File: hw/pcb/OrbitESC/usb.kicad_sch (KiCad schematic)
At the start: 5 parts, among them J1 USB_C_Receptacle_USB2.0

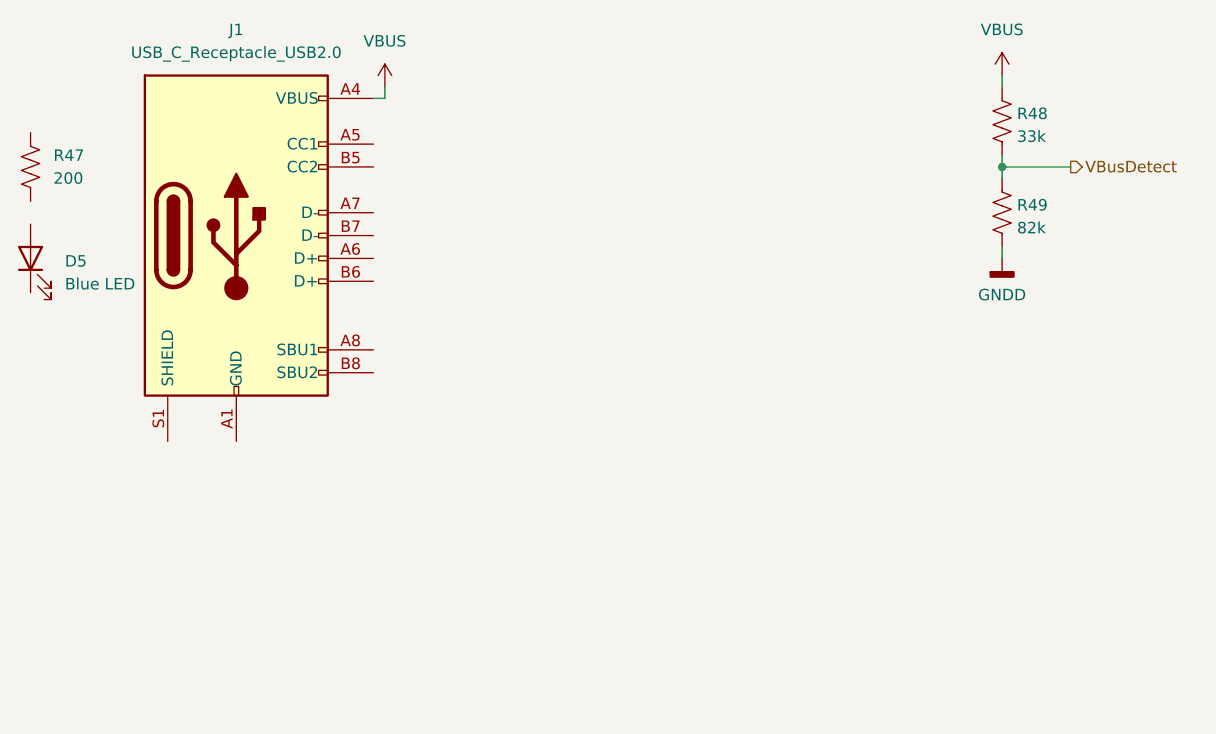
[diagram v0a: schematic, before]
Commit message: Connect USB to MCU
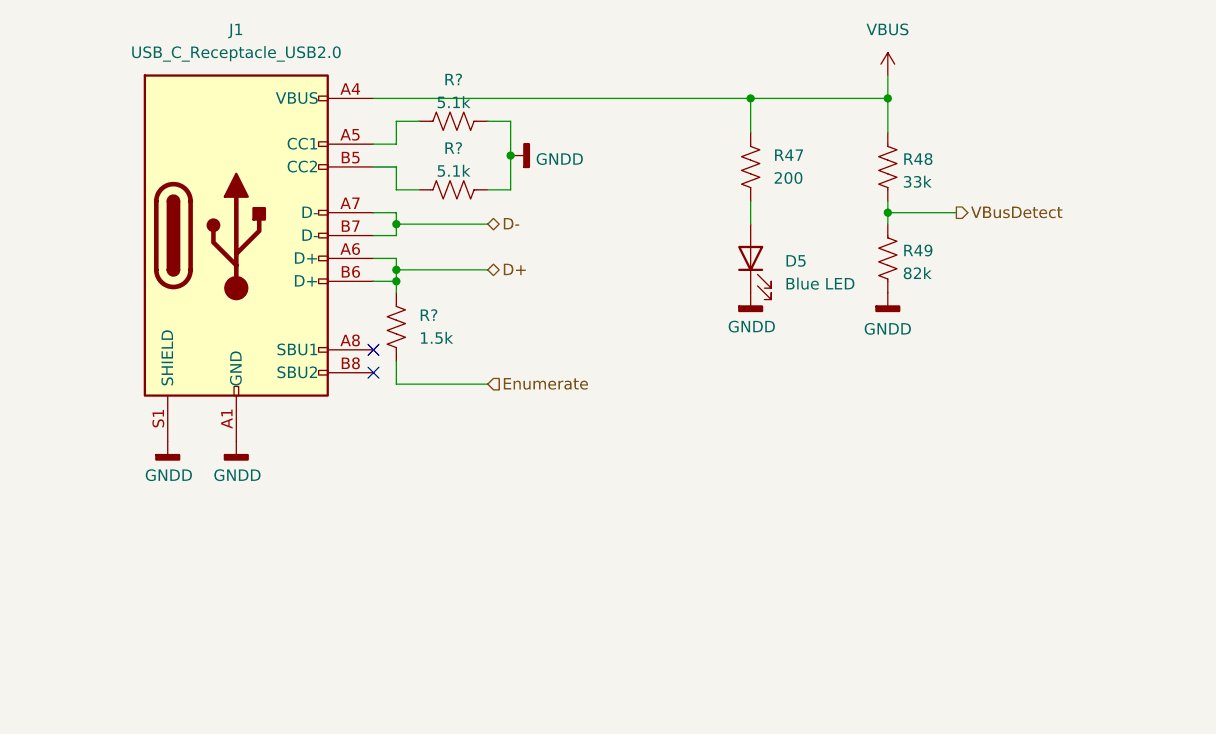
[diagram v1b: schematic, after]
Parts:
- added R? (x2): 5.1k, Resistor_SMD:R_0402_1005Metric, symbol Device:R_US
- added R?: 1.5k, Resistor_SMD:R_0402_1005Metric, symbol Device:R_US
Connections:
- net GNDD: now also D5.1 (K), J1.A1 (GND), J1.A12 (GND), J1.B1 (GND), J1.B12 (GND), J1.S1 (SHIELD), R?.2, R?.2
- net VBUS: now also R47.1
- net at R47.2: now also D5.2 (A)
- net at J1.A5 (CC1): now also R?.1
- net D+: now reaches J1.A6 (D+)
- net D+: now also J1.B6 (D+), R?.1
- net D-: now reaches J1.A7 (D-)
- net D-: now also J1.B7 (D-)
- net at J1.B5 (CC2): now also R?.1
- new net Enumerate: R?.2
- no-connect marks 0 -> 2
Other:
- moved on the sheet: D5, R47, R48, R49

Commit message: Fill out majority of schematic
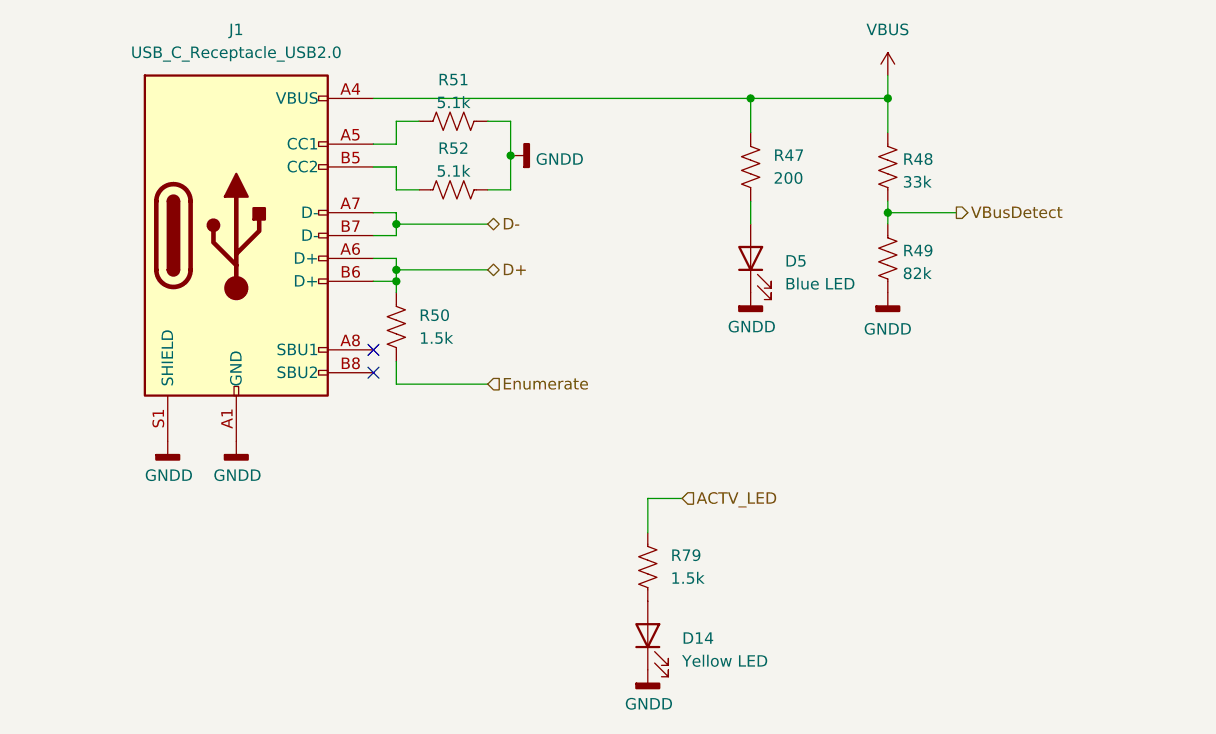
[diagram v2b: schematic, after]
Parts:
- added D14: Yellow LED, Diode_SMD:D_0603_1608Metric, symbol Device:LED
- added R79: 1.5k, Resistor_SMD:R_0402_1005Metric, symbol Device:R_US
- gave numbers to parts that had none: 3
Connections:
- net GNDD: now also D14.1 (K)
- new net: D14.2 (A), R79.2
- new net ACTV_LED: R79.1
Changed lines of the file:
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@@
+    (stroke (width 0) (type default) (color 0 0 0 0))
+  )
+  (wire (pts (xy 119.38 99.06) (xy 123.19 99.06))
     (stroke (width 0) (type default) (color 0 0 0 0))
   )
@@
     (stroke (width 0) (type default) (color 0 0 0 0))
   )
+  (wire (pts (xy 119.38 99.06) (xy 119.38 102.87))
+    (stroke (width 0) (type default) (color 0 0 0 0))
+  )
   (hierarchical_label "D-" (shape bidirectional) (at 101.6 68.58 0)
     (effects (font (size 1.27 1.27)) (justify left))
@@
     (effects (font (size 1.27 1.27)) (justify left))
   )
+  (hierarchical_label "ACTV_LED" (shape input) (at 123.19 99.06 0)
+    (effects (font (size 1.27 1.27)) (justify left))
+  )
   (hierarchical_label "D+" (shape bidirectional) (at 101.6 73.66 0)
     (effects (font (size 1.27 1.27)) (justify left))
@@
   (symbol (lib_id "Device:R_US") (at 97.79 64.77 90) (unit 1)
     (in_bom yes) (on_board yes) (fields_autoplaced)
-    (property "Reference" "R?" (id 0) (at 97.79 60.1812 90))
+    (property "Reference" "R52" (id 0) (at 97.79 60.1812 90))
     (property "Value" "5.1k" (id 1) (at 97.79 62.7181 90))
     (property "Footprint" "Resistor_SMD:R_0402_1005Metric" (id 2) (at 98.044 63.754 90)
@@
   (symbol (lib_id "Device:R_US") (at 97.79 57.15 90) (unit 1)
     (in_bom yes) (on_board yes) (fields_autoplaced)
-    (property "Reference" "R?" (id 0) (at 97.79 52.5612 90))
+    (property "Reference" "R51" (id 0) (at 97.79 52.5612 90))
     (property "Value" "5.1k" (id 1) (at 97.79 55.0981 90))
     (property "Footprint" "Resistor_SMD:R_0402_1005Metric" (id 2) (at 98.044 56.134 90)
@@
     (pin "2")
   )
+  (symbol (lib_id "power:GNDD") (at 119.38 118.11 0) (unit 1)
+    (in_bom yes) (on_board yes)
+    (property "Reference" "#PWR0128" (id 0) (at 119.38 124.46 0)
+      (effects (font (size 1.27 1.27)) hide)
+    )
+    (property "Value" "GNDD" (id 1) (at 116.84 121.92 0)
+      (effects (font (size 1.27 1.27)) (justify left))
+    )
+    (property "Footprint" "" (id 2) (at 119.38 118.11 0)
+      (effects (font (size 1.27 1.27)) hide)
+    )
+    (property "Datasheet" "" (id 3) (at 119.38 118.11 0)
+      (effects (font (size 1.27 1.27)) hide)
+    )
+    (pin "1")
+  )
   (symbol (lib_id "power:GNDD") (at 66.04 92.71 0) (unit 1)
     (in_bom yes) (on_board yes)
-    (property "Reference" "#PWR?" (id 0) (at 66.04 99.06 0)
+    (property "Reference" "#PWR040" (id 0) (at 66.04 99.06 0)
       (effects (font (size 1.27 1.27)) hide)
     )
@@
   (symbol (lib_id "Device:R_US") (at 91.44 80.01 0) (unit 1)
     (in_bom yes) (on_board yes) (fields_autoplaced)
-    (property "Reference" "R?" (id 0) (at 93.98 78.7399 0)
+    (property "Reference" "R50" (id 0) (at 93.98 78.7399 0)
       (effects (font (size 1.27 1.27)) (justify left))
     )
@@
   (symbol (lib_id "power:GNDD") (at 73.66 92.71 0) (unit 1)
     (in_bom yes) (on_board yes)
-    (property "Reference" "#PWR?" (id 0) (at 73.66 99.06 0)
+    (property "Reference" "#PWR044" (id 0) (at 73.66 99.06 0)
       (effects (font (size 1.27 1.27)) hide)
     )
@@
     (pin "1")
   )
+  (symbol (lib_id "Device:R_US") (at 119.38 106.68 0) (unit 1)
+    (in_bom yes) (on_board yes) (fields_autoplaced)
+    (property "Reference" "R79" (id 0) (at 121.92 105.4099 0)
+      (effects (font (size 1.27 1.27)) (justify left))
+    )
+    (property "Value" "1.5k" (id 1) (at 121.92 107.9499 0)
+      (effects (font (size 1.27 1.27)) (justify left))
+    )
+    (property "Footprint" "Resistor_SMD:R_0402_1005Metric" (id 2) (at 120.396 106.934 90)
+      (effects (font (size 1.27 1.27)) hide)
+    )
+    (property "Datasheet" "~" (id 3) (at 119.38 106.68 0)
+      (effects (font (size 1.27 1.27)) hide)
+    )
+    (property "JLCPCB" "C25867" (id 4) (at 119.38 106.68 0)
+      (effects (font (size 1.27 1.27)) hide)
+    )
+    (pin "1")
+    (pin "2")
+  )
   (symbol (lib_id "Device:LED") (at 130.81 72.39 90) (unit 1)
     (in_bom yes) (on_board yes) (fields_autoplaced)
@@
   (symbol (lib_id "power:GNDD") (at 130.81 76.2 0) (unit 1)
     (in_bom yes) (on_board yes)
-    (property "Reference" "#PWR?" (id 0) (at 130.81 82.55 0)
+    (property "Reference" "#PWR046" (id 0) (at 130.81 82.55 0)
       (effects (font (size 1.27 1.27)) hide)
     )
@@
   (symbol (lib_id "power:GNDD") (at 104.14 60.96 90) (unit 1)
     (in_bom yes) (on_board yes) (fields_autoplaced)
-    (property "Reference" "#PWR?" (id 0) (at 110.49 60.96 0)
+    (property "Reference" "#PWR045" (id 0) (at 110.49 60.96 0)
       (effects (font (size 1.27 1.27)) hide)
     )
@@
     (pin "1")
   )
+  (symbol (lib_id "Device:LED") (at 119.38 114.3 90) (unit 1)
+    (in_bom yes) (on_board yes) (fields_autoplaced)
+    (property "Reference" "D14" (id 0) (at 123.19 114.6174 90)
+      (effects (font (size 1.27 1.27)) (justify right))
+    )
+    (property "Value" "Yellow LED" (id 1) (at 123.19 117.1574 90)
+      (effects (font (size 1.27 1.27)) (justify right))
+    )
+    (property "Footprint" "Diode_SMD:D_0603_1608Metric" (id 2) (at 119.38 114.3 0)
+      (effects (font (size 1.27 1.27)) hide)
+    )
+    (property "Datasheet" "~" (id 3) (at 119.38 114.3 0)
+      (effects (font (size 1.27 1.27)) hide)
+    )
+    (property "JLCPCB" "C72038" (id 4) (at 119.38 114.3 90)
+      (effects (font (size 1.27 1.27)) hide)
+    )
+    (pin "1")
+    (pin "2")
+  )
   (symbol (lib_id "Device:R_US") (at 146.05 62.23 0) (unit 1)

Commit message: Schematic checklist runthrough
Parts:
- R48: footprint (none) -> Resistor_SMD:R_0402_1005Metric; JLCPCB (none) -> C25779
- R49: footprint (none) -> Resistor_SMD:R_0603_1608Metric; JLCPCB (none) -> C23254
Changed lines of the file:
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@@
       (effects (font (size 1.27 1.27)) (justify left))
     )
-    (property "Footprint" "" (id 2) (at 147.066 72.644 90)
+    (property "Footprint" "Resistor_SMD:R_0603_1608Metric" (id 2) (at 147.066 72.644 90)
       (effects (font (size 1.27 1.27)) hide)
     )
     (property "Datasheet" "~" (id 3) (at 146.05 72.39 0)
+      (effects (font (size 1.27 1.27)) hide)
+    )
+    (property "JLCPCB" "C23254" (id 4) (at 146.05 72.39 0)
       (effects (font (size 1.27 1.27)) hide)
     )
@@
       (effects (font (size 1.27 1.27)) (justify left))
     )
-    (property "Footprint" "" (id 2) (at 147.066 62.484 90)
+    (property "Footprint" "Resistor_SMD:R_0402_1005Metric" (id 2) (at 147.066 62.484 90)
       (effects (font (size 1.27 1.27)) hide)
     )
@@
       (effects (font (size 1.27 1.27)) hide)
     )
+    (property "JLCPCB" "C25779" (id 4) (at 146.05 62.23 0)
+      (effects (font (size 1.27 1.27)) hide)
+    )
